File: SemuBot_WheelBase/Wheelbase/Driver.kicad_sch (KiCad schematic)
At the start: 27 parts, among them IC1 DRV8353FSRTAR, IC4 ADS131M03IRUKT, Q1 AON7262E, Q19 AON7262E, Q2 AON7262E, Q3 AON7262E, Q5 AON7262E, Q6 AON7262E

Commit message: Encoder fix
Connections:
- net +3.3V: now also IC4.19 (AVDD)
- net GND: no longer IC4.19 (AVDD)
- net SCLK: no longer IC4.12 (SCLK)
- net SDI: no longer IC4.13 (DOUT)
- net SDO: no longer IC4.14 (DIN)
- new net SPI1_MISO: IC4.13 (DOUT)
- new net SPI1_MOSI: IC4.14 (DIN)
- new net SPI1_SCLK: IC4.12 (SCLK)
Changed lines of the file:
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@@
-	)
-	(junction
-		(at 245.11 118.11)
-		(diameter 0)
-		(color 0 0 0 0)
 	)
 	(junction
@@
 	(junction
 		(at 212.09 62.23)
+		(diameter 0)
+		(color 0 0 0 0)
+	)
+	(junction
+		(at 251.46 90.17)
 		(diameter 0)
 		(color 0 0 0 0)
@@
 	(wire
 		(pts
+			(xy 251.46 90.17) (xy 251.46 92.71)
+		)
+		(stroke
+			(width 0)
+			(type default)
+		)
+	)
+	(wire
+		(pts
 			(xy 166.37 17.78) (xy 166.37 20.32)
 		)
@@
 	(wire
 		(pts
-			(xy 251.46 86.36) (xy 251.46 92.71)
+			(xy 251.46 86.36) (xy 251.46 90.17)
 		)
 		(stroke
@@
 	(wire
 		(pts
+			(xy 242.57 90.17) (xy 251.46 90.17)
+		)
+		(stroke
+			(width 0)
+			(type default)
+		)
+	)
+	(wire
+		(pts
 			(xy 133.35 58.42) (xy 133.35 60.96)
 		)
@@
 	(wire
 		(pts
+			(xy 242.57 118.11) (xy 242.57 90.17)
+		)
+		(stroke
+			(width 0)
+			(type default)
+		)
+	)
+	(wire
+		(pts
 			(xy 140.97 109.22) (xy 143.51 109.22)
 		)
@@
 		(pts
 			(xy 161.29 41.91) (xy 163.83 41.91)
-		)
-		(stroke
-			(width 0)
-			(type default)
-		)
-	)
-	(wire
-		(pts
-			(xy 242.57 118.11) (xy 245.11 118.11)
 		)
 		(stroke
@@
 		)
 	)
-	(hierarchical_label "SCLK"
+	(hierarchical_label "SPI1_SCLK"
 		(shape input)
 		(at 264.16 133.35 0)
@@
 		)
 	)
-	(hierarchical_label "SDO"
+	(hierarchical_label "SPI1_MOSI"
 		(shape input)
 		(at 264.16 128.27 0)
@@
 		)
 	)
-	(hierarchical_label "SDI"
+	(hierarchical_label "SPI1_MISO"
 		(shape input)
 		(at 264.16 130.81 0)

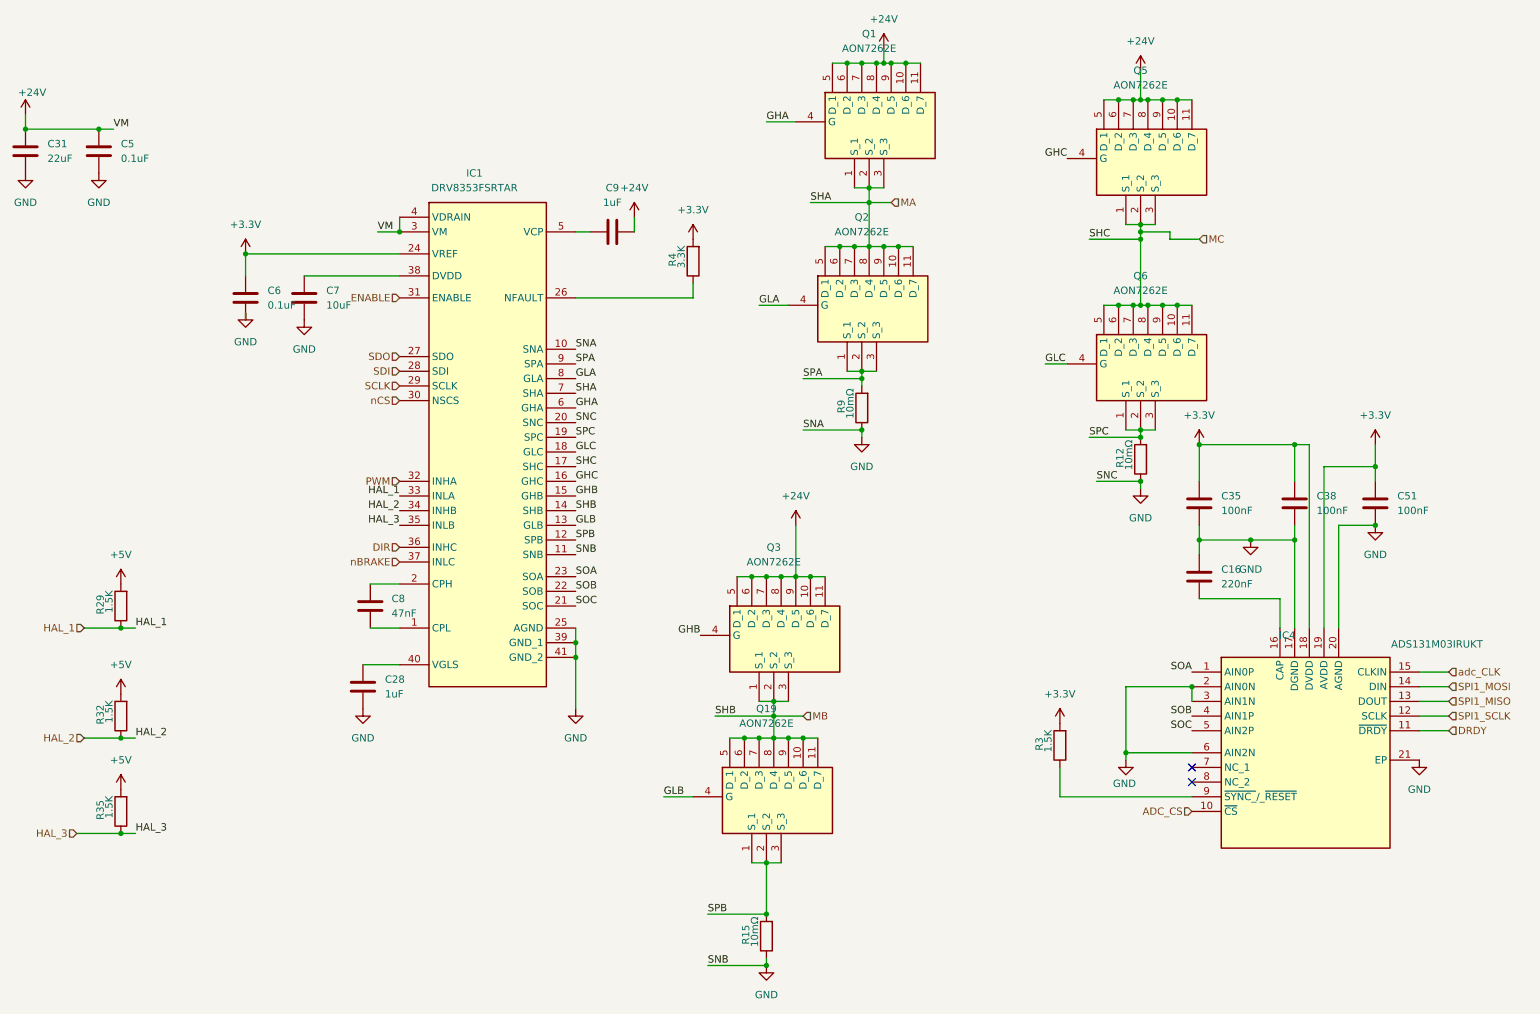
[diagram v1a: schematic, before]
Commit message: Updated mosfet symbols and organization
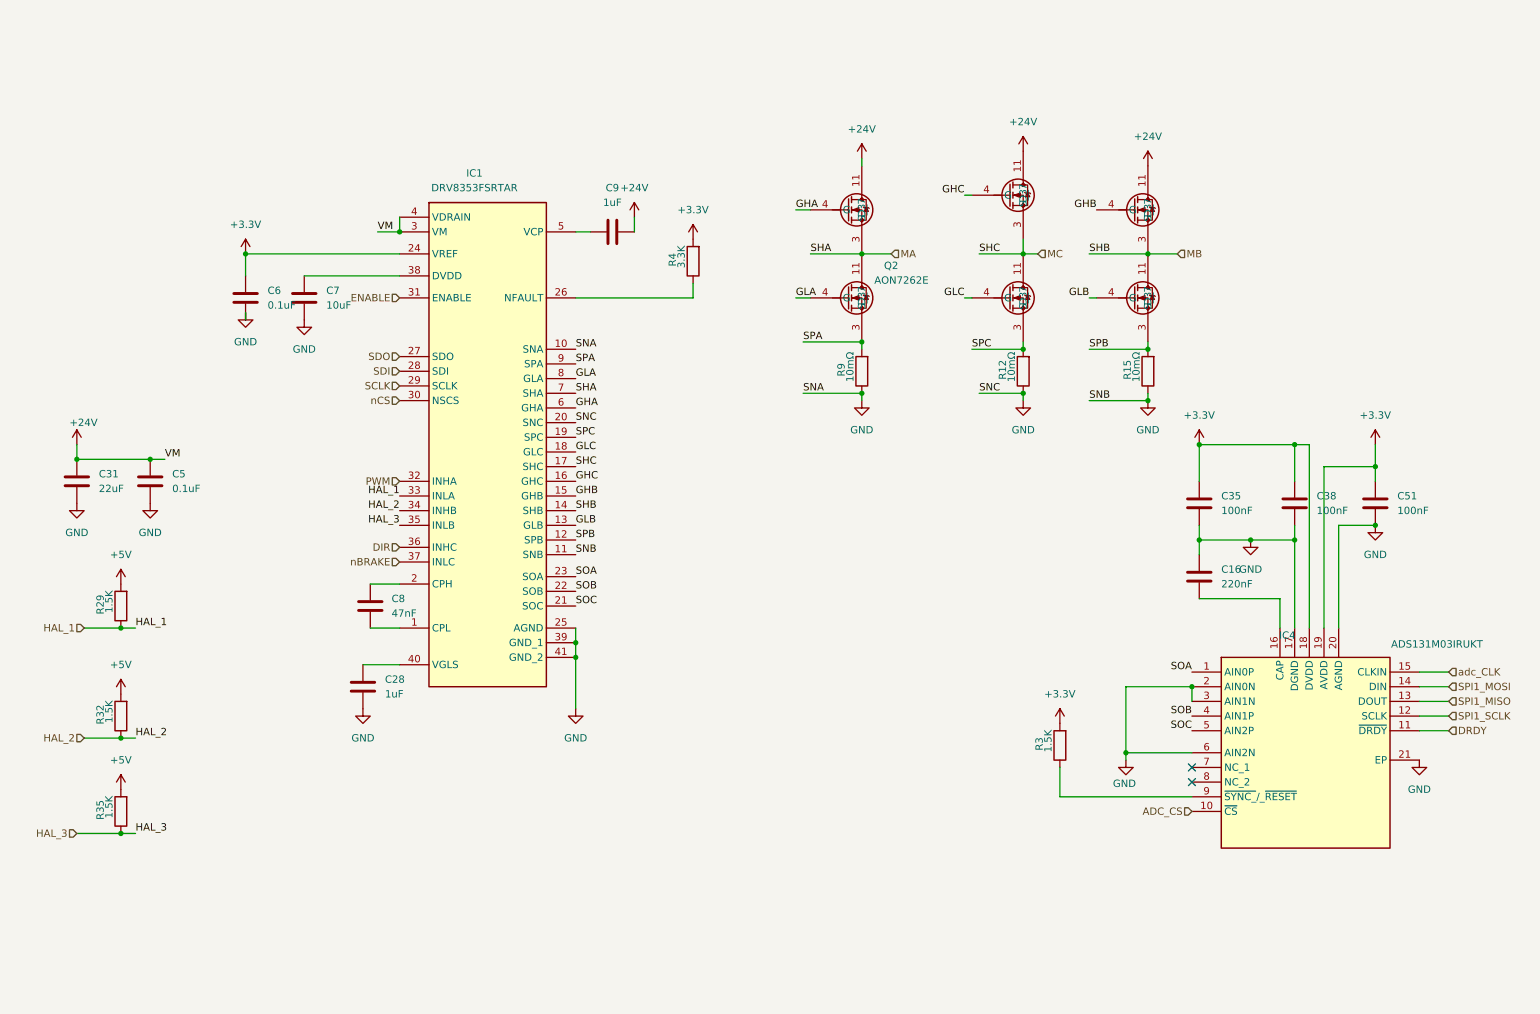
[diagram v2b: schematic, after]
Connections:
- net +24V: no longer Q1.10 (D_6), Q1.5 (D_1), Q1.6 (D_2), Q1.7 (D_3), Q1.8 (D_4), Q1.9 (D_5), Q3.10 (D_6), Q3.5 (D_1), Q3.6 (D_2), Q3.7 (D_3), Q3.8 (D_4), Q3.9 (D_5), Q5.10 (D_6), Q5.5 (D_1), Q5.6 (D_2), Q5.7 (D_3), Q5.8 (D_4), Q5.9 (D_5)
- net MA: no longer Q1.1 (S_1), Q1.2 (S_2), Q2.10 (D_6), Q2.5 (D_1), Q2.6 (D_2), Q2.7 (D_3), Q2.8 (D_4), Q2.9 (D_5)
- net MB: no longer Q19.10 (D_6), Q19.5 (D_1), Q19.6 (D_2), Q19.7 (D_3), Q19.8 (D_4), Q19.9 (D_5), Q3.1 (S_1), Q3.2 (S_2)
- net MC: no longer Q5.1 (S_1), Q5.2 (S_2), Q6.10 (D_6), Q6.5 (D_1), Q6.6 (D_2), Q6.7 (D_3), Q6.8 (D_4), Q6.9 (D_5)
- net SPA: no longer Q2.1 (S_1), Q2.2 (S_2)
- net SPB: no longer Q19.1 (S_1), Q19.2 (S_2)
- net SPC: no longer Q6.1 (S_1), Q6.2 (S_2)
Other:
- moved on the sheet: C31, C5, R12, R15, R9
